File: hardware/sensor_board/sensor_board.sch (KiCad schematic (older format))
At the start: 10 parts, among them J0 Conn_01x04, U0 HIHxx3x-021, U1 MPL115A2, U2 P82B96

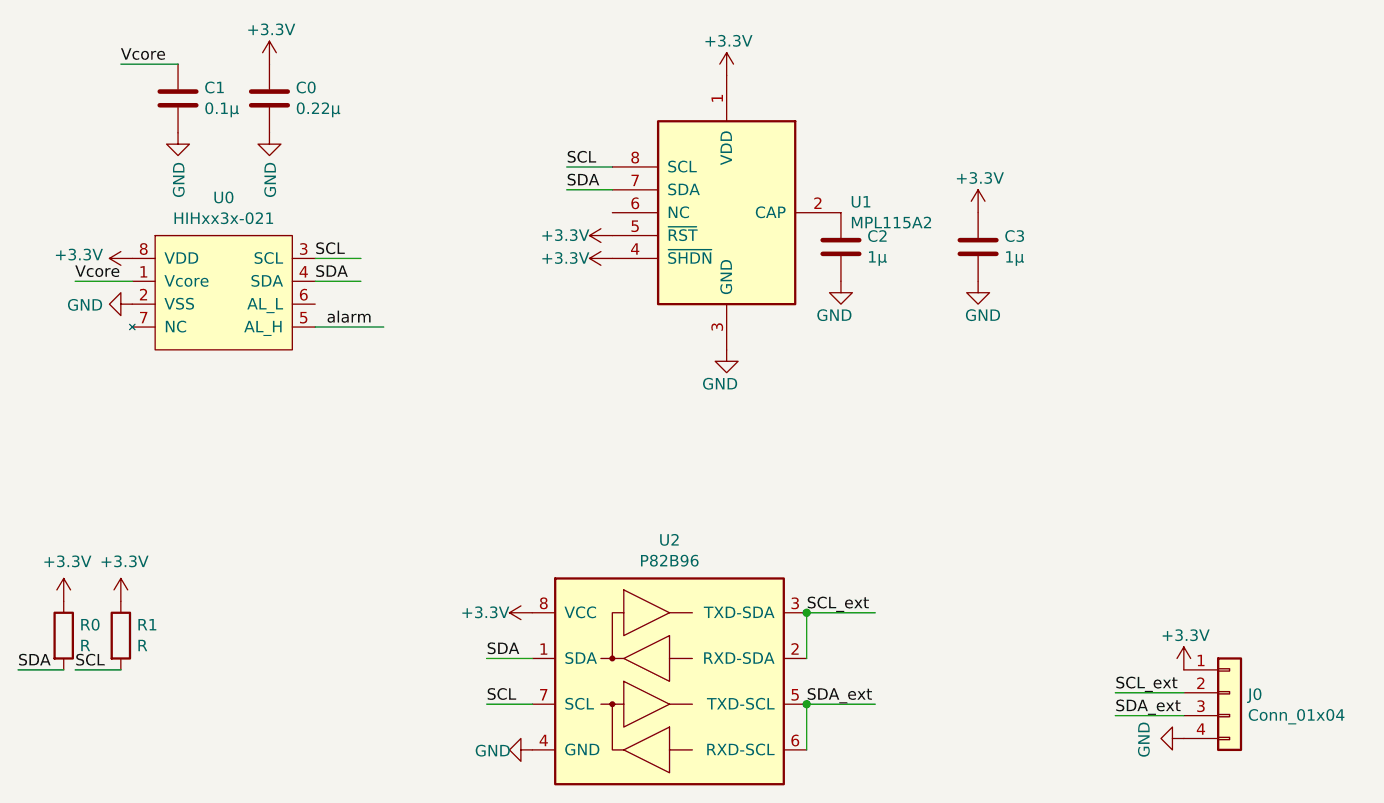
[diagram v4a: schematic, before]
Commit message: Rework of sensor board and correction of pHAT
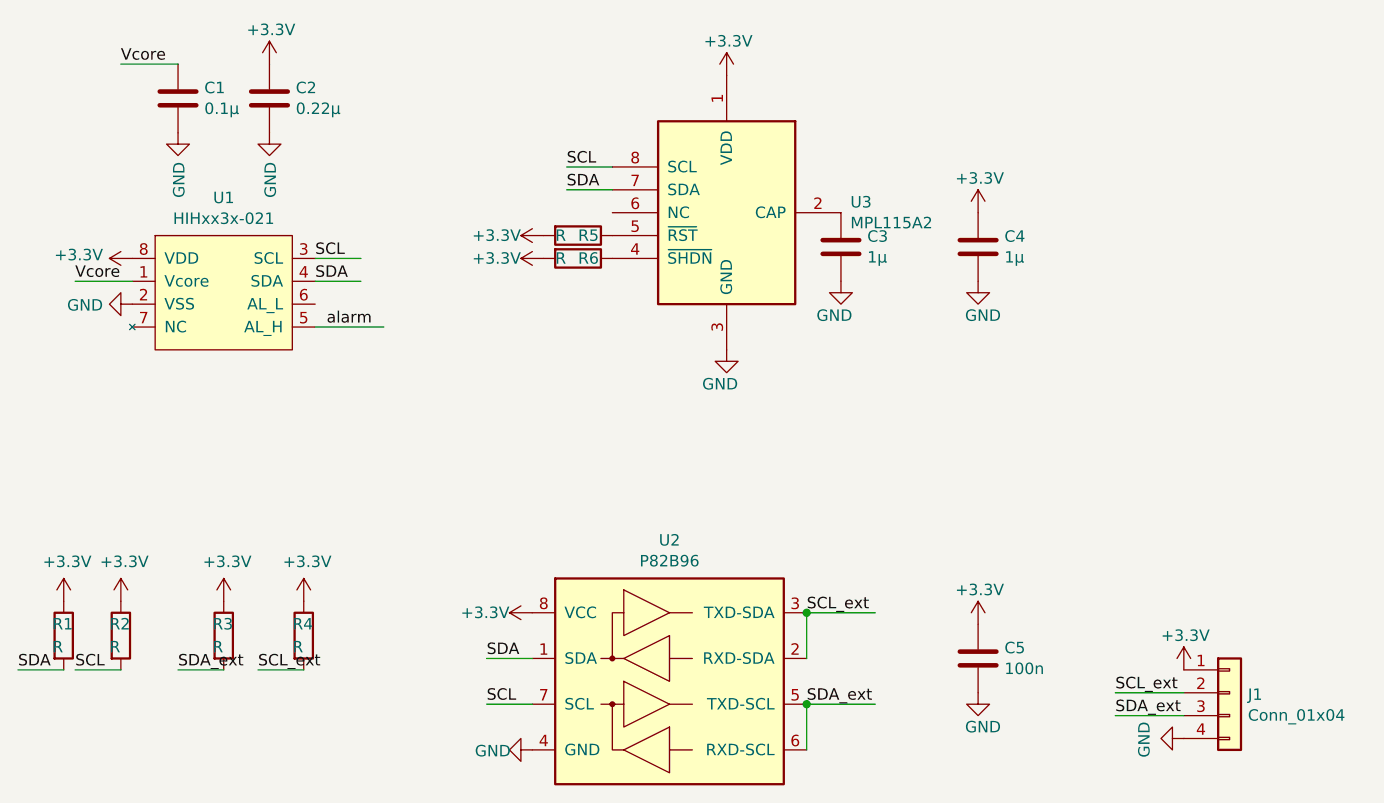
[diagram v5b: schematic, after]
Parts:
- added C5: 100n, Capacitor_SMD:C_0805_2012Metric_Pad1.15x1.40mm_HandSolder, symbol Device:C
- added R3, R4, R5, R6: R, Resistor_SMD:R_0805_2012Metric_Pad1.15x1.40mm_HandSolder, symbol Device:R
- C3: renamed from C2; footprint Capacitor_SMD:C_0805_2012Metric_Pad1.15x1.40mm_HandSolder -> Capacitor_SMD:C_1206_3216Metric_Pad1.42x1.75mm_HandSolder
- C4: renamed from C3; footprint Capacitor_SMD:C_0805_2012Metric_Pad1.15x1.40mm_HandSolder -> Capacitor_SMD:C_1206_3216Metric_Pad1.42x1.75mm_HandSolder
- renumbered C0 to C2, J0 to J1, R0 to R1, R1 to R2, U0 to U1, U1 to U3
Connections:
- wire segments 17 -> 19
